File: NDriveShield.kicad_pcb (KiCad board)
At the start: 2 copper layers, 68.6 x 53.3 mm, 35 parts, among them J1 M03, J2 M03, J3 M03, J4 M03, J5 M03, Q1 NTD5867NLT4G, Q2 NTD5867NLT4G, Q3 NTD5867NLT4G, Q4 NTD5867NLT4G, Q5 NTD5867NLT4G

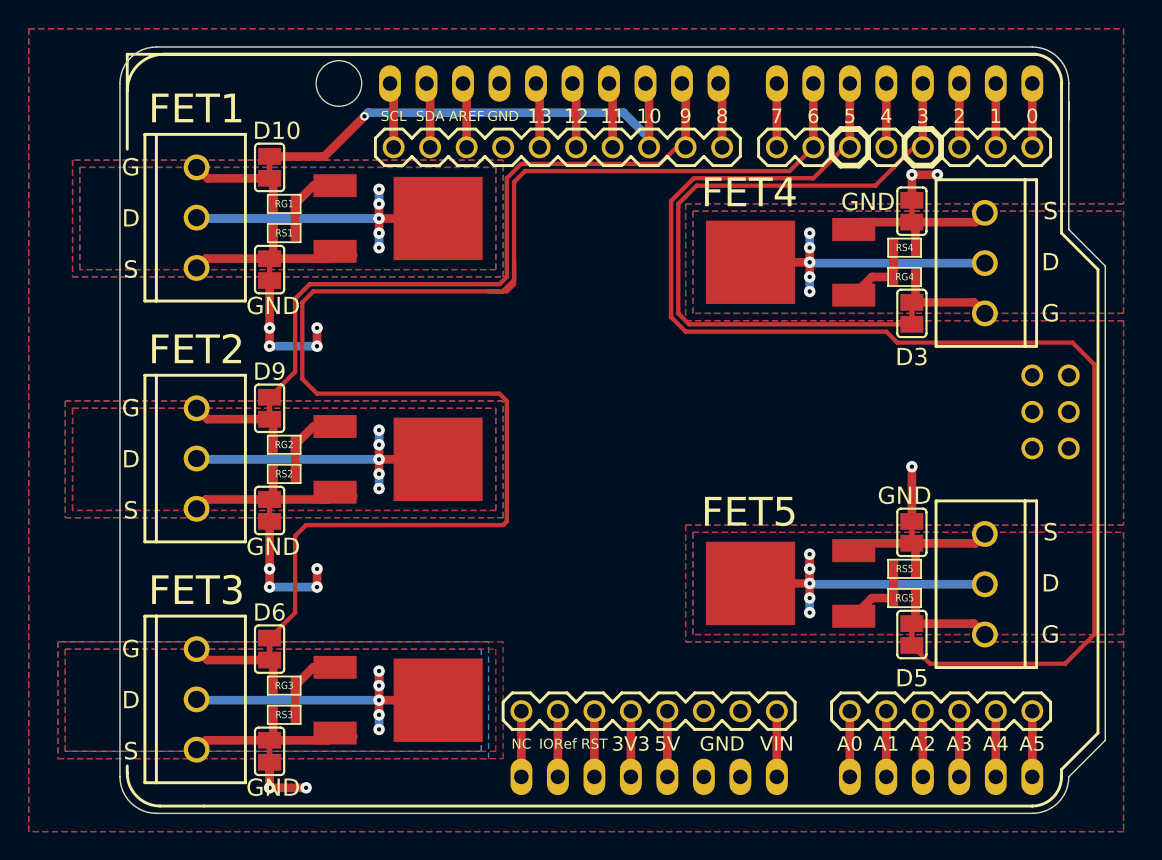
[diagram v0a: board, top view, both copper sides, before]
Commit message: NDriveShield first prototype v0.1
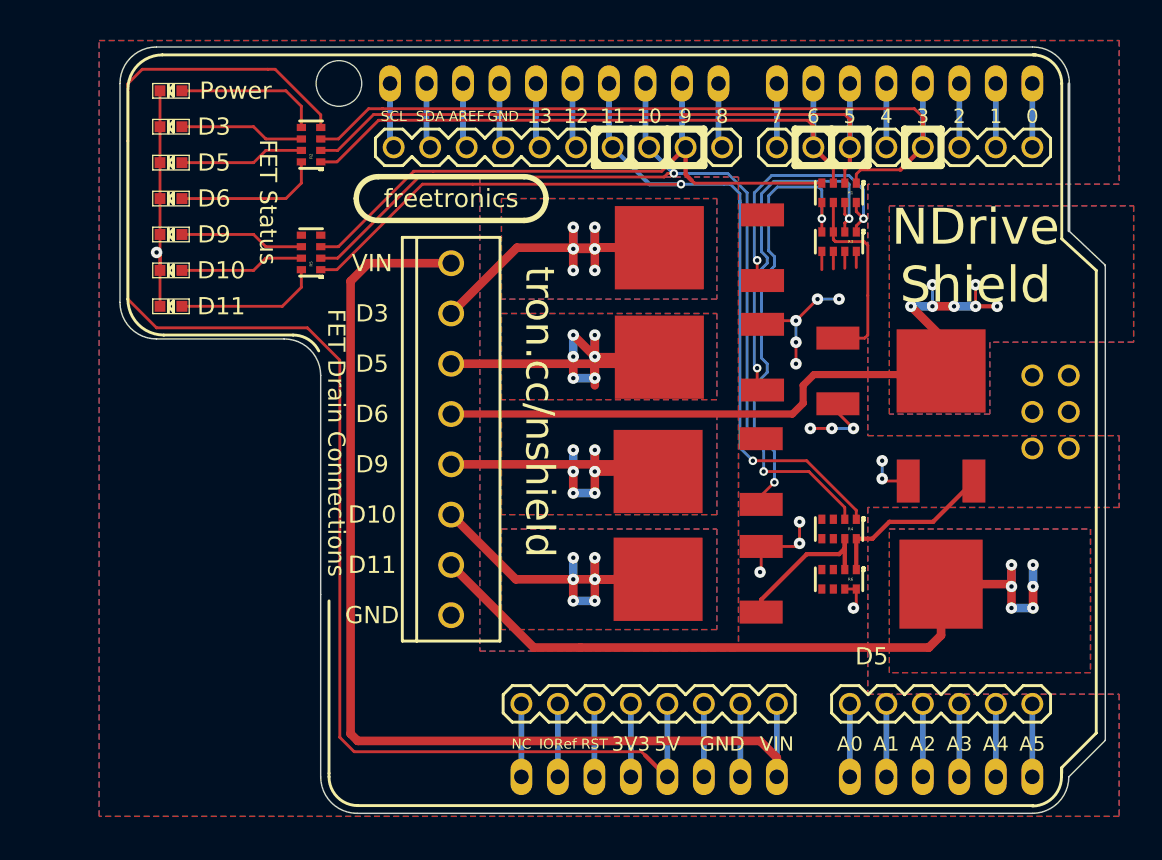
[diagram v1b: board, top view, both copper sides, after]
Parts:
- removed J1, J2, J3, J4, J5: M03, FT:SCREWTERMINAL-3.5MM-3
- removed RG1, RG2, RG3, RG4, RG5: 1K, SMD_Packages:SM0603
- removed RS1, RS2, RS3, RS4, RS5: 10K, SMD_Packages:SM0603
- removed SJG1, SJG2, SJG3, SJG4, SJG5, SJS1, SJS2, SJS3, SJS4, SJS5: SJ, FT:SJ_SHORTED
- added JP5: M08, FT:TERMINALBLOCK_3.5MM_8, F.Cu at (194.5, 59.5)
- added LED1: LED, FT:LED-0603, F.Cu at (175.0, 50.0)
- added LED2: LED, FT:LED-0603, F.Cu at (175.0, 52.5)
- added LED3: LED, FT:LED-0603, F.Cu at (175.0, 55.0)
- added LED4: LED, FT:LED-0603, F.Cu at (175.0, 57.5)
- added LED5: LED, FT:LED-0603, F.Cu at (175.0, 60.0)
- added LED6: LED, FT:LED-0603, F.Cu at (175.0, 62.5)
- added LED7: LED, FT:LED-0603, F.Cu at (175.0, 47.5)
- added LOGO_FREETRONICS: val**, FT:LOGO_FREETRONICS, F.Cu at (194.5, 55.0)
- added Q6: NTD5867NLT4G, FT:MOSFET_DPAK, F.Cu at (228.6, 78.7)
- added R1: 1K, FT:RES_CAY16, F.Cu at (221.5, 54.6)
- added R2: 500, FT:RES_CAY16, F.Cu at (184.8, 51.2)
- added R3: 10K, FT:RES_CAY16, F.Cu at (221.5, 58.0)
- added R4: 1K, FT:RES_CAY16, F.Cu at (221.5, 78.0)
- added R5: 500, FT:RES_CAY16, F.Cu at (184.8, 58.8)
- added R6: 10K, FT:RES_CAY16, F.Cu at (221.5, 81.5)
- moved Q3 41.8 mm to (225.5, 67.0)
- moved Q2 22.7 mm to (212.1, 66.0), turned to 0 degrees
- moved Q1 21.7 mm to (212.1, 58.4), turned to 0 degrees
- moved Q4 15.9 mm to (212.0, 74.0)
- moved Q5 6.45 mm to (212.0, 81.5)
- moved JP1 0.51 mm to (199.4, 90.2)
- moved JP2 0.51 mm to (222.2, 90.2)
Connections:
- net Net-(JP1-Pad2) renamed /IORef
- net Net-(JP1-Pad4) renamed /3V3
- net Net-(JP1-Pad5) renamed +5V
- net Net-(JP1-Pad8) renamed VCC
- net Net-(JP3-Pad7) renamed /D11
- Q1 pad G: Net-(Q1-PadG) -> /GATE1
- Q1 pad S: /SOURCE1 -> GND
- Q2 pad G: Net-(Q2-PadG) -> /GATE2
- Q2 pad S: /SOURCE2 -> GND
- Q3 pad G: Net-(Q3-PadG) -> /GATE3
- Q3 pad S: /SOURCE3 -> GND
- Q4 pad G: Net-(Q4-PadG) -> /GATE4
- Q4 pad S: /SOURCE4 -> GND
- Q5 pad G: Net-(Q5-PadG) -> /GATE5
- Q5 pad S: /SOURCE5 -> GND
- SHIELD1 pad SP1: Net-(SHIELD1-PadSP1) -> (no net)
- SHIELD1 pad SP2: Net-(SHIELD1-PadSP2) -> (no net)
- SHIELD1 pad SP3: Net-(SHIELD1-PadSP3) -> (no net)
- SHIELD1 pad SP4: Net-(SHIELD1-PadSP4) -> (no net)
- SHIELD1 pad SP5: Net-(SHIELD1-PadSP5) -> (no net)
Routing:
- net +5V: track 3.81 -> 102.4 mm
- net VCC: track 3.81 -> 75.3 mm
- net /D11: track 3.92 -> 70.7 mm, vias 0 -> 2
- net /D6: track 102.9 -> 44.9 mm
- net /DRAIN6: track 0.00 -> 54.5 mm, vias 0 -> 6
- net /D5: track 90.0 -> 47.2 mm
- net /D10: track 32.3 -> 67.2 mm, vias 1 -> 2
- net GND: track 31.7 -> 60.5 mm, vias 13 -> 15
- net /DRAIN3: track 22.1 -> 50.4 mm, vias 5 -> 7
- net /GATE4: track 7.28 -> 31.8 mm, vias 0 -> 2
- net /GATE2: track 7.28 -> 25.7 mm, vias 0 -> 2
- net /SOURCE1: track 12.2 -> 0.00 mm
- net /SOURCE2: track 12.2 -> 0.00 mm
- net /SOURCE3: track 12.2 -> 0.00 mm
- net /GATE1: track 7.28 -> 19.3 mm, vias 0 -> 2
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- added copper zone on B.Cu, net /DRAIN6
- added copper zone on F.Cu, net /DRAIN6
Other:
- outline, holes or cut-outs redrawn
- board text added: "(C) 2014 Freetronics Pty Ltd Licensed under TAPR Open Hardware License Designed by Angus Gratton"
- board text added: "D11"
- board text added: "FET Drain Connections"
- board text added: "FET Status"
- board text added: "NDrive Shield"
- board text added: "Power"
- board text added: "SKU: NSHIELD V0.1"
- board text added: "tron.cc/nshield"
- board text removed: "D"
- board text removed: "FET1"
- board text removed: "FET2"
- board text removed: "FET3"
- board text removed: "FET4"
- board text removed: "FET5"
- board text removed: "G"
- board text removed: "S"

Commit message: Layout cleanup, fix EtherTen/Mega/Due jack clearance, update to V1.0
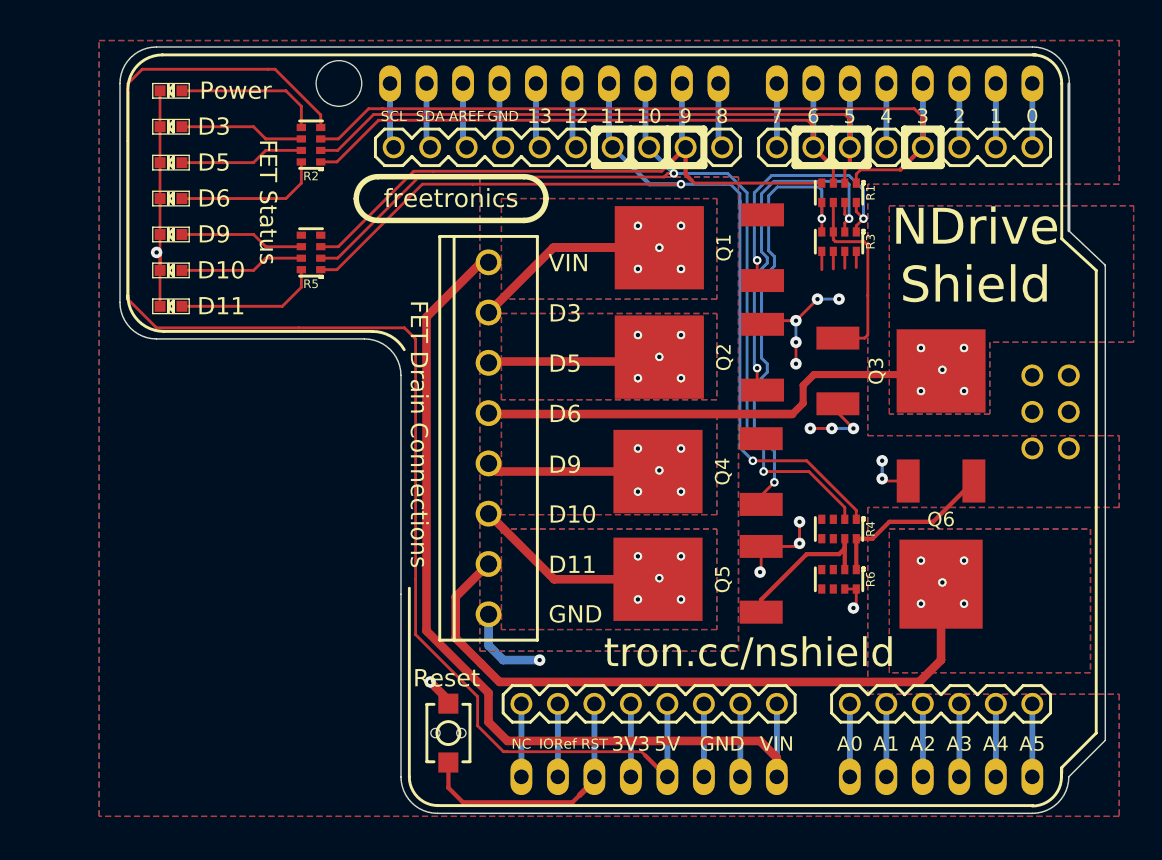
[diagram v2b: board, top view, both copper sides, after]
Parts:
- added SW1: SW_PUSHBUTTON, TACTILE_SWITCH_SMD_2PIN_TINY, F.Cu at (194.3, 92.2)
- LED7: footprint FT:LED-0603 -> LED-0603
- moved JP5 2.60 mm to (197.1, 59.4)
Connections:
- net /3V3 renamed Net-(JP1-Pad4)
- net Net-(JP1-Pad3) renamed /RESET
- net VCC renamed /VIN
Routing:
- net /DRAIN6: track 54.5 -> 71.2 mm, vias 6 -> 5
- net /RESET: track 4.57 -> 17.8 mm
- net /VIN: track 75.3 -> 62.9 mm
- net /DRAIN1: track 31.4 -> 43.4 mm, vias 6 -> 5
- net /DRAIN5: track 29.7 -> 40.5 mm, vias 6 -> 5
- net /DRAIN3: track 50.4 -> 59.8 mm, vias 7 -> 5
- net /DRAIN4: track 28.0 -> 36.8 mm, vias 6 -> 5
- net GND: track 60.5 -> 68.7 mm, vias 15 -> 17
- net /DRAIN2: track 32.3 -> 35.0 mm, vias 6 -> 5
- net +5V: track 102.4 -> 100.3 mm
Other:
- outline, holes or cut-outs redrawn
- board text added: "Reset"
- board text added: "SKU: NSHIELD V1.0"
- board text removed: "SKU: NSHIELD V0.1"

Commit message: Clean up exposed copper fill areas on bottom of board
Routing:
- net /DRAIN3: track 59.8 -> 93.3 mm
- net /DRAIN6: track 71.2 -> 85.3 mm
- net /DRAIN2: track 35.0 -> 47.0 mm
- net /DRAIN4: track 36.8 -> 48.8 mm
- net /GATE4: track 31.8 -> 24.1 mm
- net /DRAIN1: track 43.4 -> 50.8 mm
- net /DRAIN5: track 40.5 -> 47.7 mm
- net /GATE1: track 19.3 -> 18.4 mm
- net /GATE2: track 25.7 -> 25.1 mm
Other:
- board text added: "SKU: NSHIELD V1.1"
- board text removed: "SKU: NSHIELD V1.0"

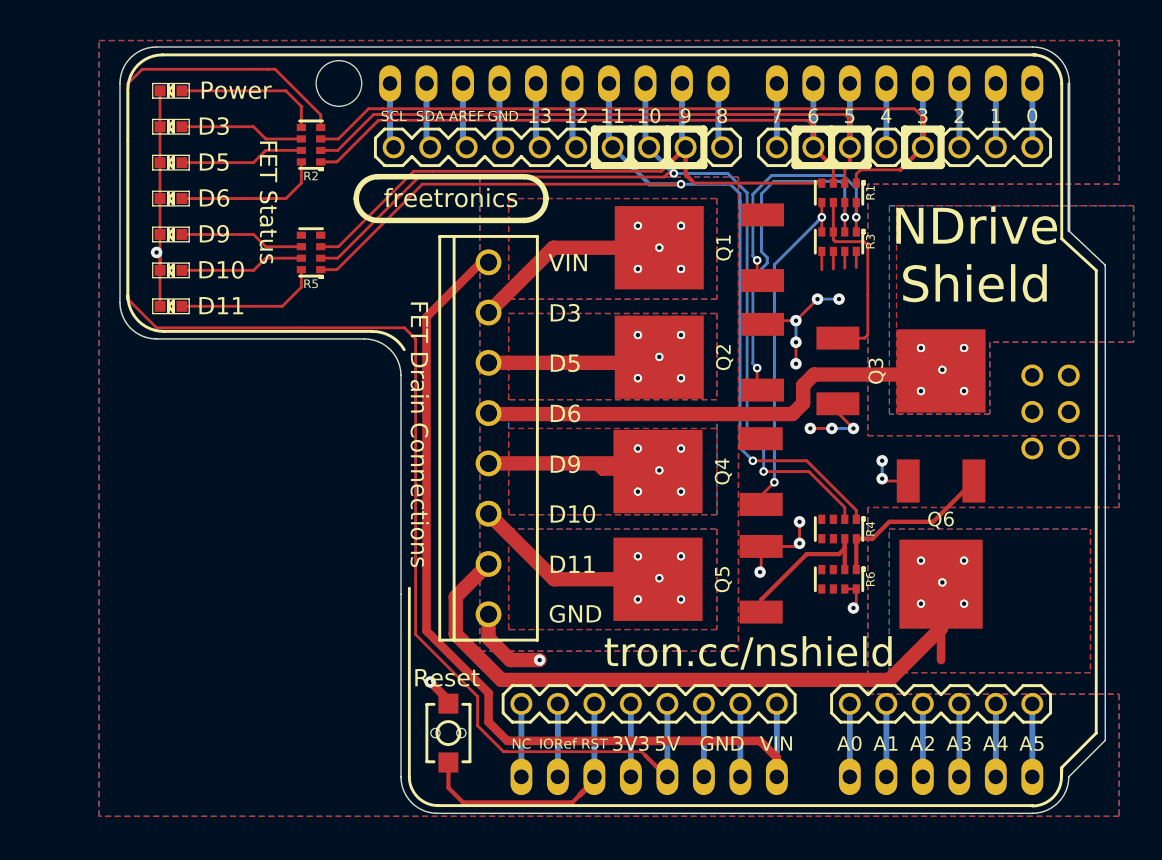
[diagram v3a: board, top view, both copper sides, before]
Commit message: Bump to V1.1, change appearance to FT-style breakout pads.
Closes #2
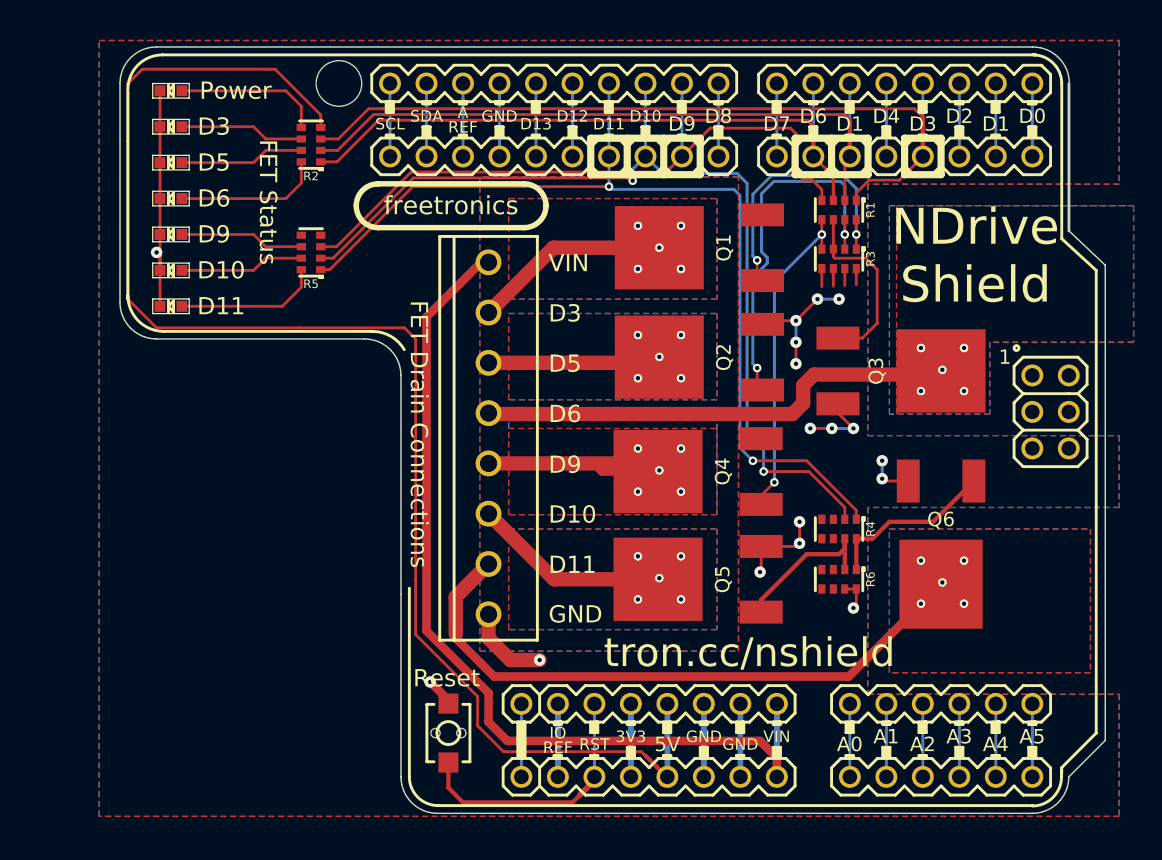
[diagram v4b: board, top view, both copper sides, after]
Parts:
- removed JP1, JP4: M08, FT:1X08
- removed JP2: M06, FT:1X06
- removed JP3: M10, FT:1X10
- R2, R5: value 500 -> 470R
- SHIELD1: footprint FT:ARDUINO_SHIELD -> FT:ARDUINO_SHIELD_ROUNDPADS_BREAKOUT
- moved R3 1.20 mm to (221.5, 59.2)
- moved R1 1.20 mm to (221.5, 55.8)
- moved LOGO_FREETRONICS 0.50 mm to (194.5, 55.5)
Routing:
- net /DRAIN6: track 85.3 -> 73.7 mm
- net /D11: track 70.7 -> 67.1 mm
- net /D9: track 44.4 -> 47.6 mm
- net /D6: track 44.9 -> 46.5 mm
- net /D5: track 47.2 -> 48.7 mm
- net /GATE1: track 18.4 -> 19.7 mm
- net /GATE2: track 25.1 -> 26.3 mm
- net /GATE4: track 24.1 -> 22.9 mm
- net /GATE3: track 13.8 -> 13.1 mm
- net GND: track 68.4 -> 68.9 mm
- net Net-(SHIELD1-PadSDA): track 4.55 -> 5.08 mm
- net Net-(SHIELD1-PadSCL): track 4.55 -> 5.08 mm
- net Net-(SHIELD1-Pad13): track 4.55 -> 5.08 mm
- net Net-(SHIELD1-Pad12): track 4.55 -> 5.08 mm
- net Net-(SHIELD1-PadAREF): track 4.55 -> 5.08 mm
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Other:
- board text removed: "(C) 2014 Freetronics Pty Ltd Licensed under TAPR Open Hardware License Designed by Angus Gratton"
- board text removed: "0"
- board text removed: "1"
- board text removed: "10"
- board text removed: "11"
- board text removed: "12"
- board text removed: "13"
- board text removed: "2"
- board text removed: "3"
- board text removed: "3V3"
- board text removed: "4"
- board text removed: "5"
- board text removed: "5V"
- board text removed: "6"
- board text removed: "7"
- board text removed: "8"
- board text removed: "9"
- board text removed: "A0"
- board text removed: "A1"
- board text removed: "A2"
- board text removed: "A3"
- board text removed: "A4"
- board text removed: "A5"
- board text removed: "AREF"
- board text removed: "IORef"
- board text removed: "NC"
- board text removed: "RST"
- board text removed: "SCL"
- board text removed: "SDA"
